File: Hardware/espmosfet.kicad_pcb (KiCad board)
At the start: 2 copper layers, 32 x 42 mm, 39 parts, among them J1 USB_B_Micro, J2 Conn_01x04_Male, J3 USB_A, J4 Conn_01x03_Male, J5 Conn_01x02_Male, J6 Conn_01x02_Male, Q1 AO3400A, Q2 AO3400A, U1 TPS2514A, U2 ESP-12E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

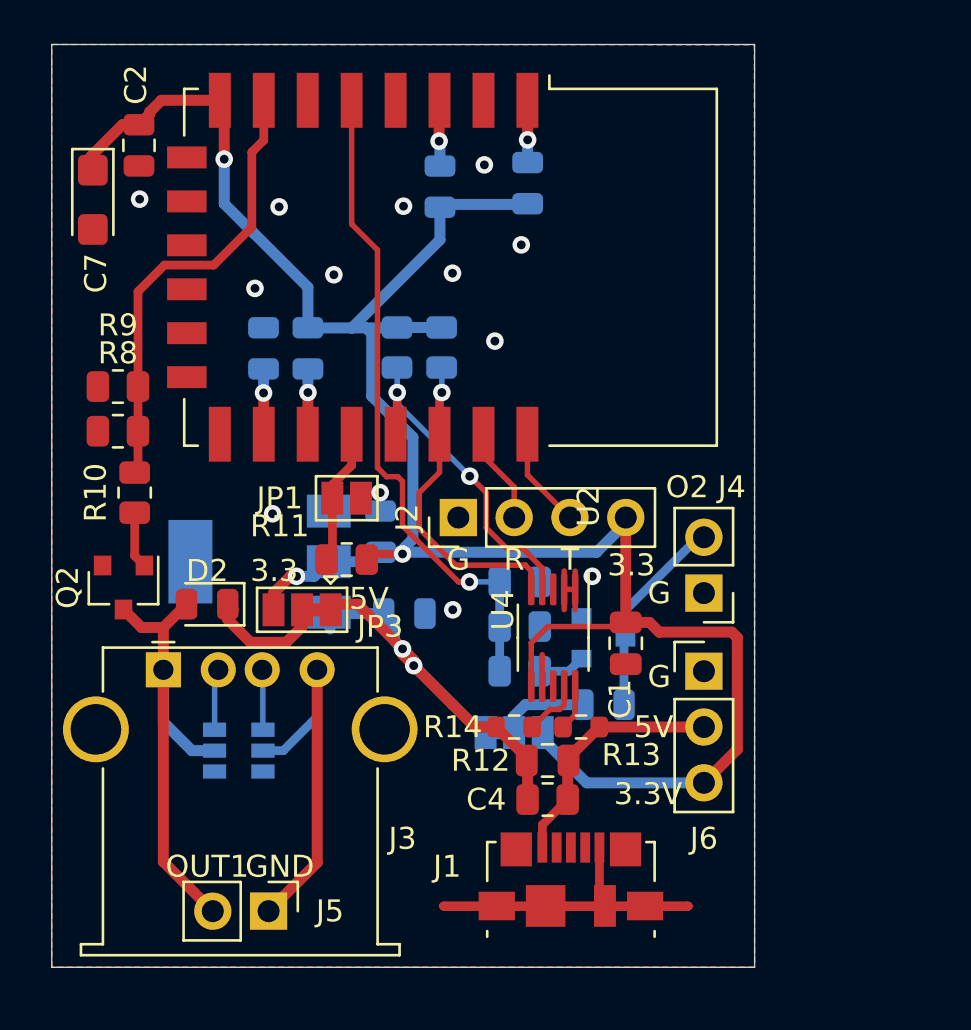
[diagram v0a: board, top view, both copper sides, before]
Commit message: update sch and pcb, fix mosfet, add 12V option, add digital led pins
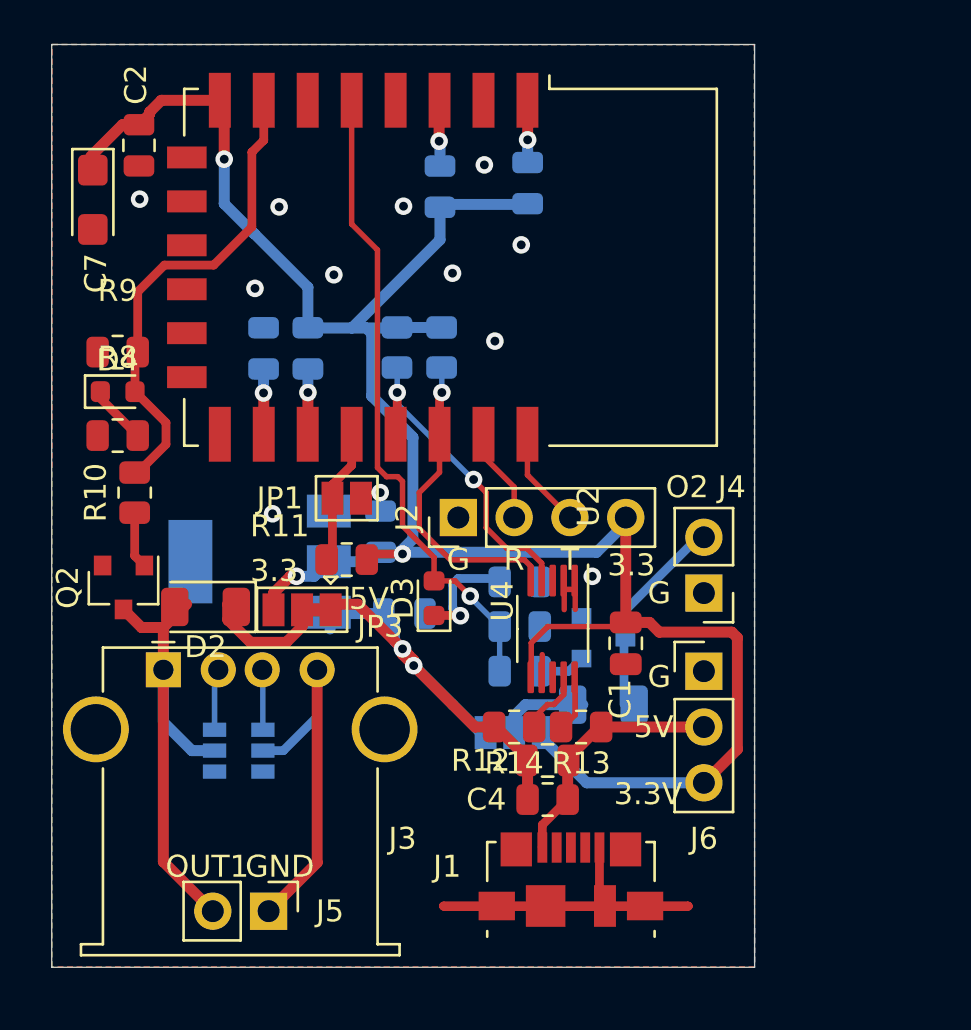
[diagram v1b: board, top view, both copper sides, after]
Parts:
- added D3: LED, LED_SMD:LED_0603_1608Metric, F.Cu at (110.4, 125.2)
- added D4: LED, LED_SMD:LED_0603_1608Metric, F.Cu at (96.0, 115.8)
- D1, D2: footprint Diode_SMD:D_0805_2012Metric -> Diode_SMD:D_1206_3216Metric
- R13, R14: footprint Resistor_SMD:R_0603_1608Metric -> Resistor_SMD:R_0805_2012Metric
- moved R9 1.57 mm to (96.0, 114.0)
- moved U4 0.40 mm to (115.8, 126.6)
- moved R8 0.20 mm to (96.0, 117.8)
- moved D2 0.15 mm to (100.0, 125.6)
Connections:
- J1 pad 2: Net-(J1-Pad2) -> unconnected-(J1-Pad2)
- J1 pad 3: Net-(J1-Pad3) -> unconnected-(J1-Pad3)
- J1 pad 4: Net-(J1-Pad4) -> unconnected-(J1-Pad4)
- R3 pad 1: /M2 -> Net-(R3-Pad1)
- R8 pad 1: /M1 -> Net-(R8-Pad1)
- U1 pad 3: Net-(U1-Pad3) -> unconnected-(U1-Pad3)
- U1 pad 4: Net-(U1-Pad4) -> unconnected-(U1-Pad4)
- U2 pad 10: Net-(U2-Pad10) -> unconnected-(U2-Pad10)
- U2 pad 11: Net-(U2-Pad11) -> unconnected-(U2-Pad11)
- U2 pad 12: Net-(U2-Pad12) -> unconnected-(U2-Pad12)
- U2 pad 13: Net-(U2-Pad13) -> unconnected-(U2-Pad13)
- U2 pad 14: Net-(U2-Pad14) -> unconnected-(U2-Pad14)
- U2 pad 2: Net-(U2-Pad2) -> unconnected-(U2-Pad2)
- U2 pad 4: Net-(U2-Pad4) -> unconnected-(U2-Pad4)
- U2 pad 6: Net-(U2-Pad6) -> unconnected-(U2-Pad6)
- U2 pad 9: Net-(U2-Pad9) -> unconnected-(U2-Pad9)
- U4 pad 3: Net-(U4-Pad3) -> unconnected-(U4-Pad3)
- U4 pad 8: Net-(U4-Pad8) -> unconnected-(U4-Pad8)
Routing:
- net Net-(R3-Pad1): track 0.00 -> 5.10 mm, vias 0 -> 1
- net Net-(R8-Pad1): track 0.00 -> 2.70 mm
- net /M1: track 20.7 -> 22.4 mm
- net /SDA: track 14.8 -> 15.8 mm
- net /M2: track 30.2 -> 29.6 mm
- net /SCL: track 14.5 -> 15.0 mm
- net GND: vias 12 -> 11
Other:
- net class Default removed

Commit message: cleanup
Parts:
- added C8: 0.1uF, Capacitor_SMD:C_0603_1608Metric, F.Cu at (103.4, 120.2)
- added C9: 0.1uF, Capacitor_SMD:C_0603_1608Metric, F.Cu at (103.4, 123.0)
- added J7: Conn_01x03_Male, Connector_PinHeader_2.54mm:PinHeader_1x03_P2.54mm_Vertical, F.Cu at (95.4, 117.0)
- added JP4: SolderJumper_3_Bridged12, Jumper:SolderJumper-3_P1.3mm_Bridged12_Pad1.0x1.5mm, F.Cu at (101.4, 131.8)
- added JP5: SolderJumper_3_Bridged12, Jumper:SolderJumper-3_P1.3mm_Bridged12_Pad1.0x1.5mm, F.Cu at (119.6, 134.4)
- added R17: 150, Resistor_SMD:R_0805_2012Metric, F.Cu at (98.2, 120.4)
- added U5: SN74LVC1T45DBV, Package_TO_SOT_SMD:SOT-23-6, F.Cu at (101.0, 121.6)
- J4: value Conn_01x03_Male -> Conn_01x04_Male; footprint Connector_PinHeader_2.54mm:PinHeader_1x03_P2.54mm_Vertical -> Connector_PinHeader_2.54mm:PinHeader_1x04_P2.54mm_Horizontal
- U2: value ESP-12E -> ESP-12F
- moved R10 6.34 mm to (97.4, 114.1), turned to 180 degrees
- moved D4 6.02 mm to (97.6, 110.0)
- moved R9 6.02 mm to (97.6, 108.2)
- moved R8 5.97 mm to (97.4, 112.0)
- moved C7 3.67 mm to (94.8, 103.4)
- moved J5 2.75 mm to (100.1, 139.4), turned to 90 degrees
- moved C2 1.90 mm to (97.6, 102.8)
- moved R15 1.79 mm to (110.2, 112.8)
- moved R16 1.79 mm to (112.2, 112.8)
- moved R4 1.77 mm to (106.2, 113.0)
- moved R5 1.77 mm to (104.2, 113.0)
- moved U2 1.74 mm to (112.8, 109.6)
- moved J1 1.39 mm to (116.6, 139.4)
- moved R12 1.03 mm to (115.6, 135.4)
- moved Q2 0.93 mm to (96.0, 125.6)
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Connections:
- net Net-(R4-Pad2) renamed /GPIO2
- J3 pad 1: /O1 -> +5V
- J3 pad 4: GND -> /O1
- J5 pad 1: GND -> Net-(J5-Pad1)
- J6 pad 1: GND -> Net-(J6-Pad1)
- U1 pad 5: /O1 -> +5V
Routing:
- net +5V: track 25.1 -> 73.1 mm, vias 2 -> 5
- net +3V3: track 101.0 -> 118.2 mm, vias 3 -> 4
- net GND: track 47.6 -> 30.5 mm
- net /O1: track 22.7 -> 38.8 mm, vias 0 -> 1
- net Net-(J6-Pad1): track 0.00 -> 15.0 mm, vias 0 -> 1
- net /GPIO2: track 2.99 -> 17.0 mm, vias 1 -> 2
- net Net-(Q2-Pad1): track 2.59 -> 14.9 mm
- net Net-(J5-Pad1): track 0.00 -> 8.13 mm
- net /M1: track 22.4 -> 17.4 mm
- net +12V: track 0.00 -> 3.27 mm
- net Net-(J7-Pad2): track 0.00 -> 2.82 mm
- net /GPIO0: track 6.17 -> 8.67 mm
- net /SCL: track 15.0 -> 16.8 mm
- net Net-(R17-Pad2): track 0.00 -> 1.80 mm
- net Net-(R1-Pad2): track 3.02 -> 4.24 mm
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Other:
- board text added: "5"
- board text added: "D"
- board text added: "Flash"

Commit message: add USB-C input
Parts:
- added P1: USB_C_Receptacle_USB2.0, Connector_USB:USB_C_Receptacle_XKB_U262-16XN-4BVC11, F.Cu at (115.4, 139.0)
- added R18: 10k, Resistor_SMD:R_0805_2012Metric, F.Cu at (111.2, 132.5)
- added R19: 10k, Resistor_SMD:R_0805_2012Metric, B.Cu at (116.8, 139.3)
- added R20: 10k, Resistor_SMD:R_0805_2012Metric, B.Cu at (114.8, 139.3)
- moved JP5 6.11 mm to (122.8, 139.6)
- moved R12 2.82 mm to (113.8, 133.2)
- moved R13 2.51 mm to (119.2, 130.2)
- moved C4 1.29 mm to (116.5, 132.5), turned to -90 degrees
- moved J1 1.20 mm to (115.4, 139.4)
- moved JP2 1.08 mm to (114.0, 132.4)
- moved R14 0.63 mm to (113.8, 130.8)
- moved U4 0.40 mm to (115.8, 126.6)
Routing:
- net GND: track 30.5 -> 5.44 mm, vias 11 -> 16
- net +5VD: track 12.3 -> 26.8 mm
- net Net-(P1-PadS1): track 0.00 -> 11.2 mm
- net +5V: track 73.1 -> 80.3 mm
- net +12V: track 3.27 -> 7.79 mm
- net Net-(P1-PadA5): track 0.00 -> 3.48 mm, vias 0 -> 1
- net Net-(P1-PadB5): track 0.00 -> 3.20 mm, vias 0 -> 1
- net Net-(P1-PadA6): track 0.00 -> 2.77 mm
- net Net-(P1-PadA7): track 0.00 -> 2.68 mm
- net Net-(J6-Pad1): track 15.0 -> 16.5 mm
- net Net-(D1-Pad1): track 4.10 -> 5.18 mm
- net Net-(R14-Pad1): track 3.46 -> 4.19 mm
- net Net-(R13-Pad2): track 2.23 -> 2.85 mm
- net +3V3: track 118.2 -> 117.5 mm
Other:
- board text added: "12V"
- board text added: "ESP-12x USB Mosfet Switch Digital LED control V2"

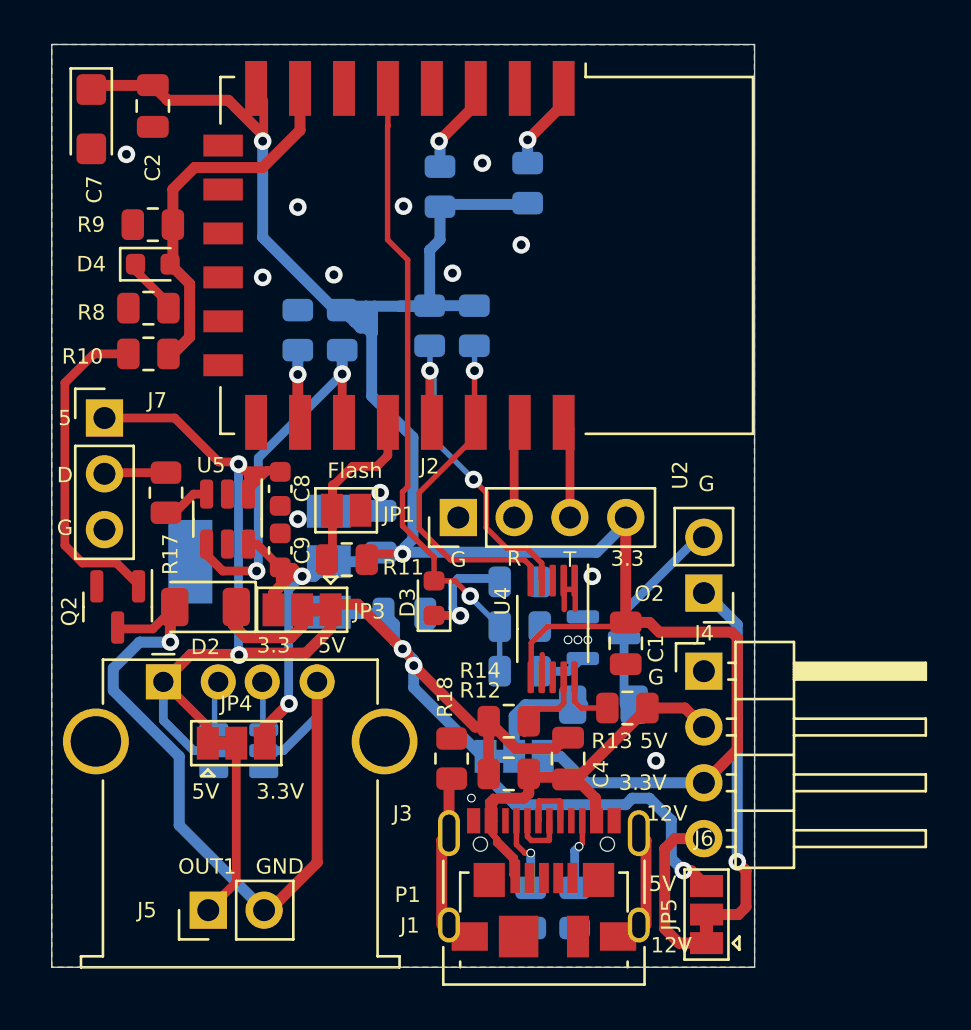
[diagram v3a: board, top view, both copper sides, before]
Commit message: add ws2812b on board, add USB-C Output
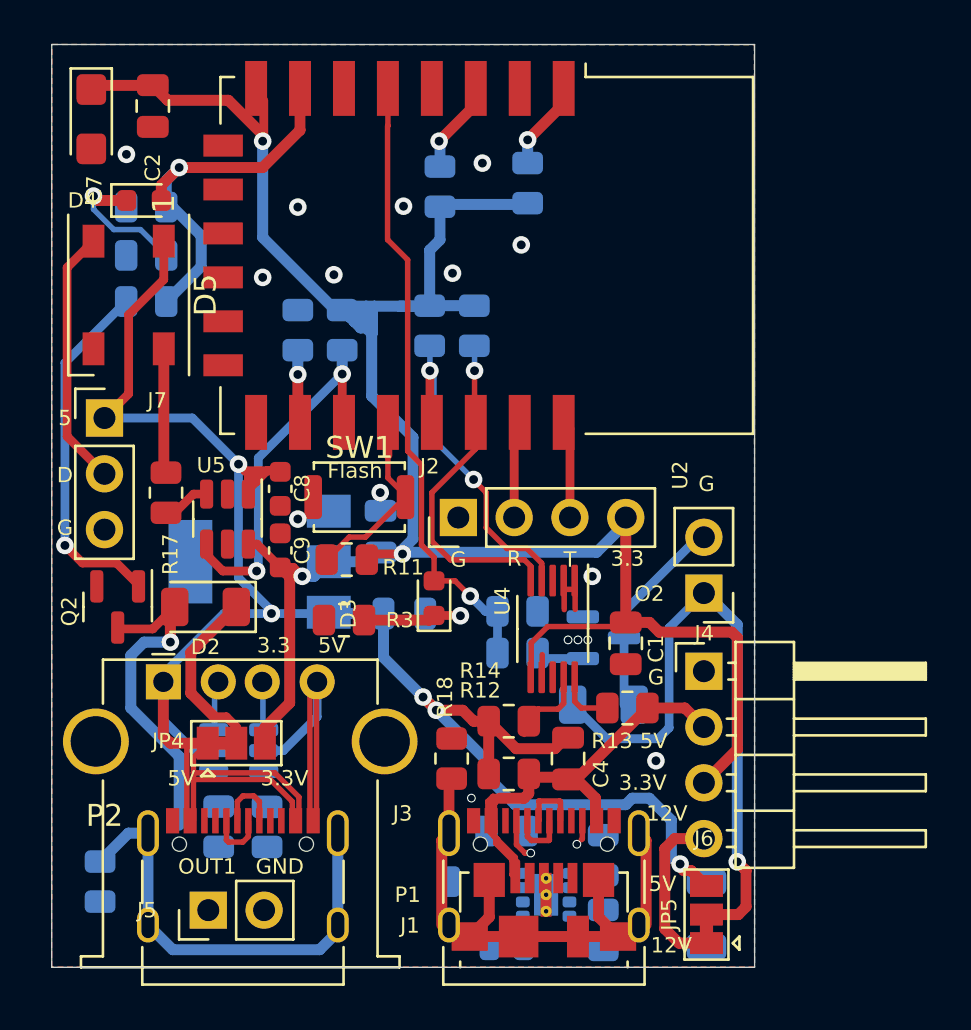
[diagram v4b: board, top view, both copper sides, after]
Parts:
- removed JP1: Jumper_2_Open, Jumper:SolderJumper-2_P1.3mm_Open_Pad1.0x1.5mm
- removed JP2, JP3: SolderJumper_3_Bridged12, Jumper:SolderJumper-3_P1.3mm_Bridged12_Pad1.0x1.5mm
- added C10: 22uF, Capacitor_SMD:C_1206_3216Metric, B.Cu at (122.8, 139.6)
- added C6: 10uF, Capacitor_SMD:C_0603_1608Metric, B.Cu at (113.7, 141.2)
- added D5: WS2812B, LED_SMD:LED_WS2812B_PLCC4_5.0x5.0mm_P3.2mm, F.Cu at (96.5, 111.4)
- added P2: USB_C_Receptacle_USB2.0, Connector_USB:USB_C_Receptacle_XKB_U262-16XN-4BVC11, F.Cu at (101.7, 139.0)
- added R21: 523k, Resistor_SMD:R_0805_2012Metric, B.Cu at (118.1, 136.9)
- added R22: 100k, Resistor_SMD:R_0805_2012Metric, B.Cu at (118.1, 140.3)
- added R23: 1M, Resistor_SMD:R_0805_2012Metric, B.Cu at (95.2, 138.1)
- added R24: 5.11k, Resistor_SMD:R_0805_2012Metric, B.Cu at (102.8, 135.6)
- added R25: 5.11k, Resistor_SMD:R_0805_2012Metric, B.Cu at (100.6, 135.6)
- added SW1: SW_Push, Button_Switch_SMD:SW_Push_SPST_NO_Alps_SKRK, F.Cu at (107.0, 120.6)
- added U6: TPS82140, Package_LGA:Texas_SIL0008D_MicroSiP-8-1EP_2.8x3mm_P0.65mm_EP1.1x1.9mm_ThermalVias, B.Cu at (115.5, 138.7)
- R10, R8, R9: moved to B.Cu
- R18: value 10k -> 1M
- R19, R20: value 10k -> 5.11k
- R3: moved to F.Cu
- moved R3 8.19 mm to (106.3, 126.2), turned to 180 degrees
- moved R19 4.68 mm to (113.7, 135.8), turned to 180 degrees
- moved R20 3.05 mm to (112.0, 138.1), turned to 180 degrees
- moved D4 2.93 mm to (97.2, 107.1)
- moved R8 2.40 mm to (97.3, 109.6)
- moved R10 2.39 mm to (97.3, 111.7)
- moved R9 0.85 mm to (97.3, 107.4)
- moved R7 0.83 mm to (114.2, 127.7)
- moved R6 0.70 mm to (114.2, 125.8)
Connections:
- D1 pad 1: Net-(D1-Pad1) -> /O2V
- D2 pad 1: Net-(D2-Pad1) -> /O1V
- J1 pad 6: GND -> /Shield
- J5 pad 1: Net-(J5-Pad1) -> /O1V
- J6 pad 1: Net-(J6-Pad1) -> /O2V
- JP4 pad 2: Net-(J5-Pad1) -> /O1V
- JP5 pad 2: Net-(J6-Pad1) -> /O2V
- P1 pad S1: Net-(P1-PadS1) -> /Shield
- R17 pad 1: Net-(J7-Pad2) -> Net-(R17-Pad1)
- R18 pad 2: Net-(P1-PadS1) -> /Shield
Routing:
- net /O2V: track 0.00 -> 28.5 mm, vias 0 -> 1
- net /Shield: track 0.00 -> 23.8 mm
- net +5V: track 80.3 -> 102.0 mm
- net /Shield1: track 0.00 -> 20.8 mm
- net Net-(J6-Pad1): track 16.5 -> 0.00 mm, vias 1 -> 0
- net Net-(P1-PadS1): track 11.2 -> 0.00 mm
- net +3V3: track 117.5 -> 106.7 mm, vias 4 -> 3
- net /O1: track 38.8 -> 28.2 mm
- net Net-(J7-Pad2): track 2.82 -> 11.9 mm
- net /O1V: track 0.00 -> 8.24 mm
- net Net-(J5-Pad1): track 8.13 -> 0.00 mm
- net Net-(R17-Pad1): track 0.00 -> 5.68 mm
- net GND: track 5.44 -> 10.7 mm
- net Net-(D1-Pad1): track 5.18 -> 0.00 mm
- net Net-(D2-Pad1): track 5.03 -> 0.00 mm
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
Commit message: update to V2 Version
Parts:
- removed R21: 523k, Resistor_SMD:R_0805_2012Metric
- removed R22: 100k, Resistor_SMD:R_0805_2012Metric
- C10: footprint Capacitor_SMD:C_1206_3216Metric -> Capacitor_SMD:C_0805_2012Metric
- R19, R20, R24, R25: footprint Resistor_SMD:R_0805_2012Metric -> Resistor_SMD:R_0603_1608Metric
- U6: value TPS82140 -> LMZM23601V5; footprint Package_LGA:Texas_SIL0008D_MicroSiP-8-1EP_2.8x3mm_P0.65mm_EP1.1x1.9mm_ThermalVias -> Package_LGA:Texas_SIL0010A_MicroSiP-10-1EP_3.8x3mm_P0.6mm_EP0.7x2.9mm_ThermalVias
- moved C10 10.0 mm to (112.8, 139.2)
- moved C6 4.68 mm to (118.3, 140.3), turned to 90 degrees
- moved R20 3.87 mm to (113.2, 134.4), turned to 90 degrees
- moved R19 1.87 mm to (115.5, 135.6)
- moved U6 0.41 mm to (115.6, 139.1), turned to 90 degrees
- moved JP4 0.05 mm to (101.4, 131.8)
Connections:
- U6 pad 1: +12V -> GND
- U6 pad 2: +12V -> GND
- U6 pad 3: GND -> +12V
- U6 pad 4: +5VD -> +12V
- U6 pad 5: +5VD -> unconnected-(U6-Pad5)
- U6 pad 6: Net-(R21-Pad1) -> +5VD
- U6 pad 7: unconnected-(U6-Pad7) -> +5VD
- U6 pad 9: GND -> unconnected-(U6-Pad9)
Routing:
- net /O1: track 28.2 -> 55.6 mm
- net /O1V: track 8.24 -> 29.1 mm, vias 0 -> 2
- net +5V: track 102.0 -> 114.6 mm
- net +12V: track 7.79 -> 15.6 mm, vias 0 -> 1
- net +5VD: track 26.8 -> 31.5 mm, vias 0 -> 3
- net Net-(P2-PadA5): track 0.00 -> 3.43 mm, vias 0 -> 1
- net Net-(P2-PadB5): track 0.00 -> 2.87 mm, vias 0 -> 1
- net Net-(P1-PadA5): track 1.89 -> 3.98 mm
- net Net-(P1-PadB5): track 0.89 -> 2.64 mm
- net GND: track 10.7 -> 12.1 mm, vias 16 -> 33
- net Net-(D4-Pad1): track 6.38 -> 6.94 mm
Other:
- board text added: "Out1"
- board text added: "Out2"
